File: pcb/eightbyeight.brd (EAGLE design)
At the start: 60 x 60 mm, 140 parts, among them CON1 USB_MICROSMT+THRUHULE, Q1 16MHz, SW1 SWITCH_SPDT, SW2 BRIGHTNESS, U1 MK20DN64VFM5, U10 FDG6316P, U11 FDG6316P, U12 FDG6316P, U2 ICN2026, U3 74138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

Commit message: Update board TODOs
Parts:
- R11: value 50 -> 47
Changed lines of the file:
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@@
 <layer number="13" name="Route13" color="4" fill="5" visible="no" active="no"/>
 <layer number="14" name="Route14" color="1" fill="6" visible="no" active="no"/>
-<layer number="15" name="Route" color="5" fill="1" visible="no" active="yes"/>
+<layer number="15" name="Route" color="5" fill="1" visible="yes" active="yes"/>
 <layer number="16" name="Bottom" color="1" fill="1" visible="no" active="yes"/>
 <layer number="17" name="Pads" color="10" fill="1" visible="yes" active="yes"/>
-<layer number="18" name="Vias" color="10" fill="1" visible="no" active="yes"/>
+<layer number="18" name="Vias" color="10" fill="1" visible="yes" active="yes"/>
 <layer number="19" name="Unrouted" color="6" fill="1" visible="no" active="yes"/>
 <layer number="20" name="Dimension" color="15" fill="1" visible="yes" active="yes"/>
@@
 <attribute name="VALUE" x="4.2" y="12.284" size="1.016" layer="27" rot="R180"/>
 </element>
-<element name="R11" library="adafruit" package="R0805" value="50" x="12" y="4.8" smashed="yes" rot="R180">
+<element name="R11" library="adafruit" package="R0805" value="47" x="12" y="4.8" smashed="yes" rot="R180">
 <attribute name="NAME" x="12.762" y="3.784" size="1.27" layer="25" rot="R180"/>
 <attribute name="VALUE" x="10.262" y="5.386" size="1.27" layer="27" rot="R180"/>

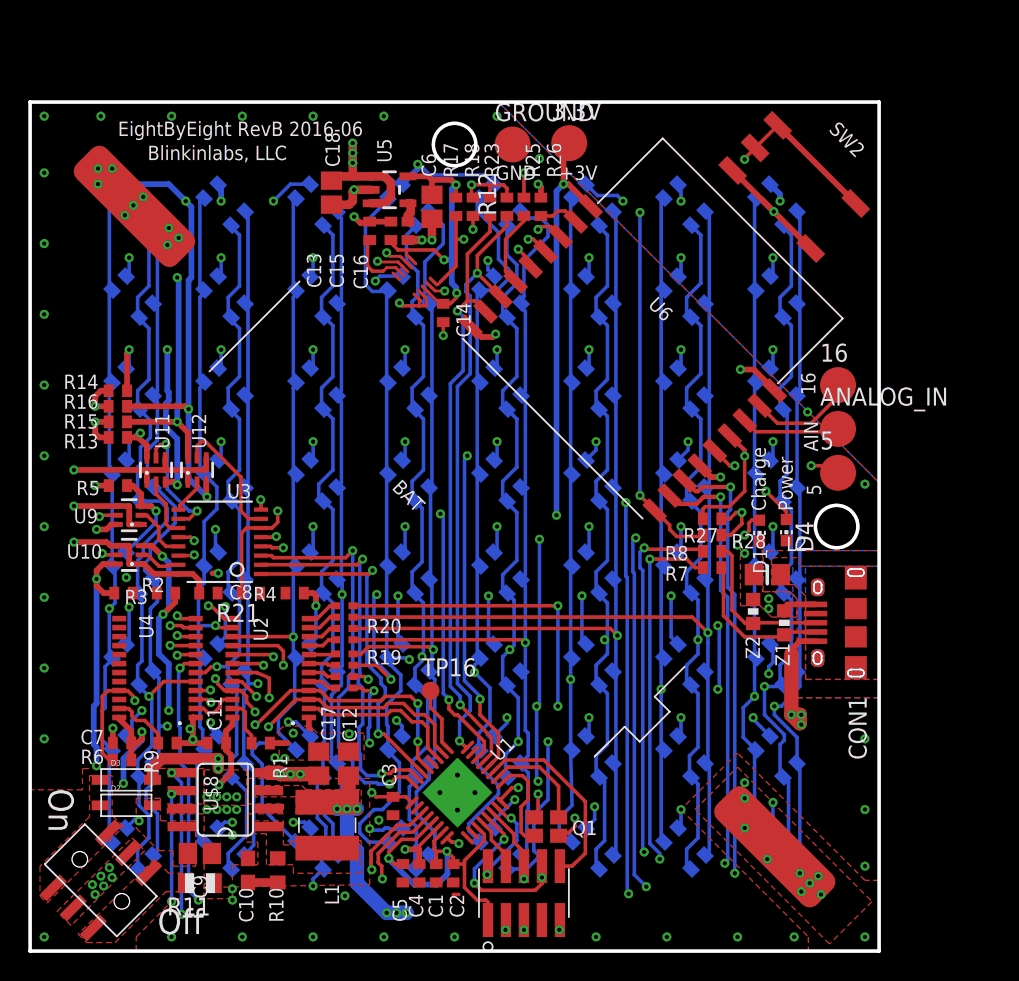
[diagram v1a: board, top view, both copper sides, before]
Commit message: Test pads in progress
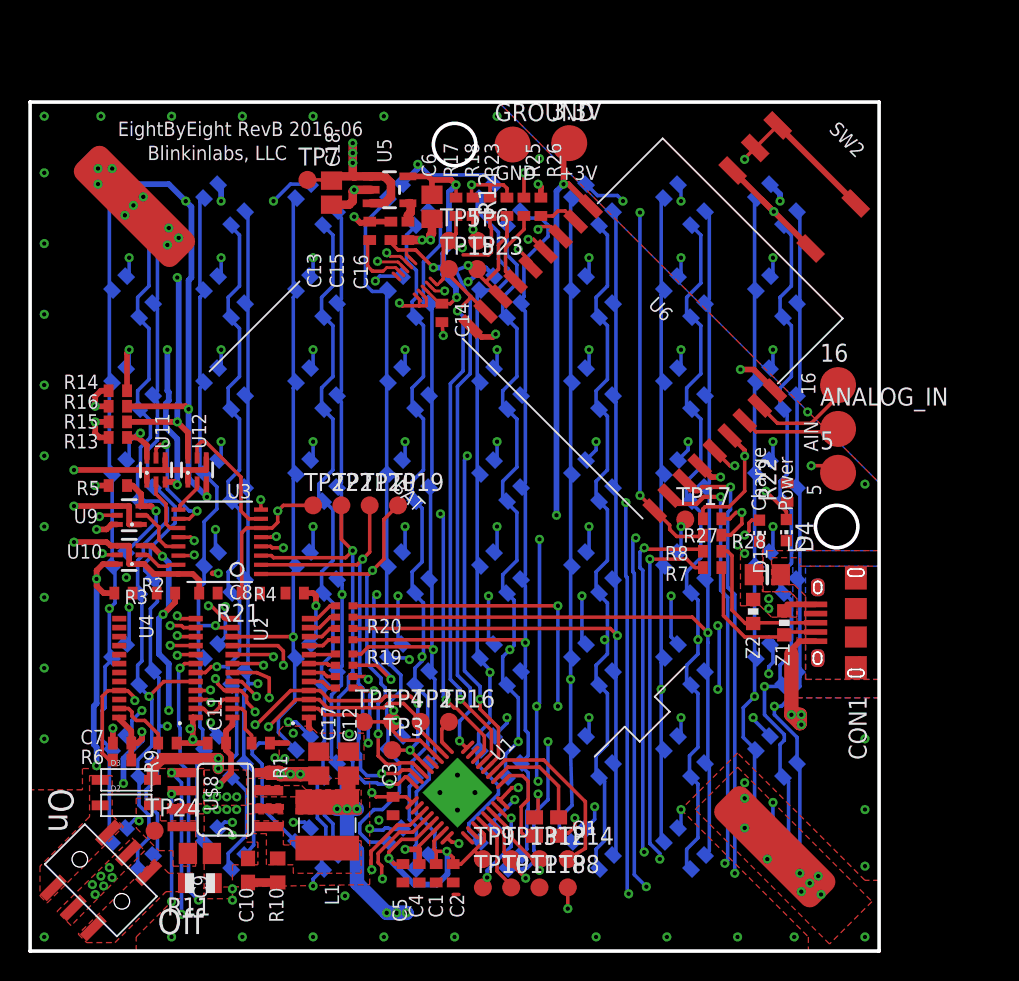
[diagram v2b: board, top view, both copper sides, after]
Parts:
- removed U$2: JTAG_ARM_10PIN, blinkinlabs:2X05-1.27MM-SMD
- added R22: 100, adafruit:R0402
- added TP1, TP10, TP11, TP12, TP13, TP14, TP15, TP17, TP18, TP19, TP2, TP20, TP21, TP22, TP23, TP24, TP3, TP4, TP5, TP6, TP7, TP8, TP9: PTR1B1,27, testpad:B1,27
- C16: value 470pF -> 47pF
- D1: value BLUE -> ORANGE
- D4: value BLUE -> PURPLE
- R12, R23, R25, R26, R27, R6: value 10k -> 47k
- R21: value 2k 1% -> 47k
- R28: value 10k -> DNP
- moved TP16 2.56 mm to (29.6, 16.2)
- moved C14 0.10 mm to (29.1, 45.1)
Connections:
- new net N$1: D1.C, D4.C, R22.2
- net +5V: now also TP7.TP
- net ARM_3V3: now also TP9.TP; no longer U$2.P$1
- net ARM_RESET: now also TP14.TP; no longer U$2.P$10
- net ARM_RX: now also TP13.TP; no longer U$2.P$8
- net ARM_RX1: now also TP23.TP
- net ARM_TCK: now also TP11.TP; no longer U$2.P$4
- net ARM_TMS: now also TP10.TP; no longer U$2.P$2
- net ARM_TX: now also TP12.TP; no longer U$2.P$6
- net BOOST_5V: now also TP24.TP
- net ESP_GPIO0: now also TP15.TP
- net ESP_RESET: now also TP17.TP
- net GND: now also R22.1, TP18.TP; no longer D1.C, D4.C, U$2.P$3, U$2.P$5, U$2.P$9
- net I2C_SCL: now also TP6.TP
- net I2C_SDA: now also TP5.TP
- net LED_CLK: now also TP2.TP
- net LED_DAT_0: now also TP1.TP
- net LED_HS_EN: now also TP22.TP
- net LED_OE: now also TP4.TP
- net LED_ROW_A: now also TP19.TP
- net LED_ROW_B: now also TP20.TP
- net LED_ROW_C: now also TP21.TP
- net LED_STB: now also TP3.TP
- net VBAT: now also TP8.TP
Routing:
- net LED_ROW_A: track 24.7 -> 31.0 mm
- net ARM_RX: track 57.4 -> 51.7 mm, vias 5 -> 3
- net ARM_3V3: track 68.5 -> 64.2 mm
- net LED_ROW_B: track 27.1 -> 31.2 mm
- net LED_ROW_C: track 28.1 -> 31.6 mm
- net LED_HS_EN: track 38.3 -> 40.9 mm
- net ARM_RX1: track 42.6 -> 45.0 mm
- net ARM_BOOTLOADER: track 4.49 -> 2.16 mm
- net GND: track 92.7 -> 90.8 mm, vias 91 -> 88
- net +5V: track 138.6 -> 140.3 mm
- net LED_STB: track 23.2 -> 24.8 mm
- net ARM_TCK: track 3.74 -> 5.40 mm
- net VBAT: track 45.1 -> 46.6 mm, vias 15 -> 16
- net ARM_TX: track 50.6 -> 49.4 mm
- net LED_DAT_0: track 11.6 -> 10.5 mm
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
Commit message: Closer to RevD
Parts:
- removed L2: 130ohm @100MHz, blinkinlabs:0805
- removed R22: 100, adafruit:R0402
- added SJ1: SOLDERJUMPERTRACE, SparkFun-Passives:SJ_2S-TRACE
- added TP25: PTR1B1,27, testpad:B1,27
- added Z3: PGB1010603, PaxInstrument-T400:SPARKFUN-RESISTORS_0603-RES
- moved Z2 0.47 mm to (51.0, 24.4)
- moved Z1 0.45 mm to (53.1, 23.6)
- moved TP17 0.30 mm to (46.0, 30.5)
- moved TP15 0.22 mm to (29.8, 48.3)
- moved TP23 0.22 mm to (31.8, 48.3)
- moved TP5 0.22 mm to (29.8, 50.3)
- moved TP6 0.22 mm to (31.8, 50.3)
- moved D1 0.20 mm to (51.5, 29.9)
- moved D4 0.20 mm to (53.5, 29.9)
- moved TP1 0.10 mm to (23.7, 16.2)
- moved TP16 0.10 mm to (29.7, 16.2)
- moved TP2 0.10 mm to (27.7, 16.2)
- moved TP3 0.10 mm to (25.7, 14.2)
- moved TP4 0.10 mm to (25.7, 16.2)
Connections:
- removed net BUTTON1: R28.1, SW2.1, SW2.2, U6.IO4
- removed net SHIELD: CON1.PAD$1, CON1.PAD$10, CON1.PAD$2, CON1.PAD$3, CON1.PAD$4, CON1.PAD$5, CON1.PAD$6, CON1.PAD$7, CON1.PAD$8, CON1.PAD$9, L2.1
- new net BUTTON: R28.1, SW2.1, SW2.2, TP25.TP, U6.IO4
- net GND: now also CON1.PAD$1, CON1.PAD$10, CON1.PAD$2, CON1.PAD$3, CON1.PAD$4, CON1.PAD$5, CON1.PAD$6, CON1.PAD$7, CON1.PAD$8, CON1.PAD$9, SJ1.1, Z3.1; no longer L2.2, R22.1
- net N$1: now also SJ1.2; no longer R22.2
- net USB_5V: now also Z3.2
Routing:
- net BUTTON: track 0.00 -> 45.3 mm, vias 0 -> 3
- net BUTTON1: track 44.5 -> 0.00 mm, vias 3 -> 0
- net GND: track 90.8 -> 74.9 mm, vias 88 -> 94
- net N$1: track 0.00 -> 3.69 mm
- net BCOL2: track 56.4 -> 54.6 mm
- net ESP_RESET: track 51.6 -> 53.1 mm
- net USB_D-: track 52.3 -> 51.0 mm
- net USB_D+: track 52.2 -> 51.0 mm
- net 1ROW1: track 74.3 -> 73.1 mm
- net ESP_GPIO0: track 44.0 -> 45.3 mm
- net ARM_RX1: track 45.0 -> 43.9 mm
- net N$9: track 11.2 -> 10.3 mm
- net RCOL3: track 54.5 -> 55.3 mm
- net ACC_INT1: track 14.2 -> 15.0 mm
- net BCOL6: track 79.0 -> 79.7 mm
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- removed copper zone on layer 1, net SHIELD
- removed copper zone on layer 16, net SHIELD
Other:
- board text added: "EightByEight RevD 2016-07"
- board text removed: "EightByEight RevB 2016-06"

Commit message: Final RevD
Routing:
- net GND: vias 94 -> 104
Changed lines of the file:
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@@
 <via x="58.9" y="28.3" extent="1-16" drill="0.3"/>
 <via x="55.1" y="28.2" extent="1-16" drill="0.3"/>
+<via x="17.2" y="37.8" extent="1-16" drill="0.3"/>
+<via x="23.6" y="44.8" extent="1-16" drill="0.3"/>
+<via x="32.7" y="37.4" extent="1-16" drill="0.3"/>
+<via x="36.2" y="44.6" extent="1-16" drill="0.3"/>
+<via x="49.2" y="40" extent="1-16" drill="0.3"/>
+<via x="36" y="31.9" extent="1-16" drill="0.3"/>
+<via x="26.1" y="26.2" extent="1-16" drill="0.3"/>
+<via x="36.7" y="19.9" extent="1-16" drill="0.3"/>
+<via x="39.1" y="11.8" extent="1-16" drill="0.3"/>
+<via x="45.5" y="11.2" extent="1-16" drill="0.3"/>
 </signal>
 <signal name="LED_STB">

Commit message: Clean up board silkscreen
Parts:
- R1: value 2k 1% -> 1.8k 1%
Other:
- board text added: "3.3V"
- board text removed: "+3V"

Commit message: Small updates from further testing
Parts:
- R1: value 1.8k 1% -> 1.6k 1%
- R12, R23, R25, R26, R27: value 47k -> 10k
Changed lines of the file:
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@@
 <layer number="13" name="Route13" color="4" fill="5" visible="no" active="no"/>
 <layer number="14" name="Route14" color="1" fill="6" visible="no" active="no"/>
-<layer number="15" name="Route" color="5" fill="1" visible="no" active="yes"/>
-<layer number="16" name="Bottom" color="1" fill="1" visible="no" active="yes"/>
-<layer number="17" name="Pads" color="10" fill="1" visible="no" active="yes"/>
-<layer number="18" name="Vias" color="10" fill="1" visible="no" active="yes"/>
+<layer number="15" name="Route" color="5" fill="1" visible="yes" active="yes"/>
+<layer number="16" name="Bottom" color="1" fill="1" visible="yes" active="yes"/>
+<layer number="17" name="Pads" color="10" fill="1" visible="yes" active="yes"/>
+<layer number="18" name="Vias" color="10" fill="1" visible="yes" active="yes"/>
 <layer number="19" name="Unrouted" color="6" fill="1" visible="no" active="yes"/>
 <layer number="20" name="Dimension" color="15" fill="1" visible="yes" active="yes"/>
@@
 <layer number="25" name="tNames" color="11" fill="1" visible="no" active="yes"/>
 <layer number="26" name="bNames" color="7" fill="1" visible="no" active="yes"/>
-<layer number="27" name="tValues" color="11" fill="1" visible="yes" active="yes"/>
+<layer number="27" name="tValues" color="11" fill="1" visible="no" active="yes"/>
 <layer number="28" name="bValues" color="7" fill="1" visible="no" active="yes"/>
-<layer number="29" name="tStop" color="7" fill="3" visible="no" active="yes"/>
+<layer number="29" name="tStop" color="7" fill="3" visible="yes" active="yes"/>
 <layer number="30" name="bStop" color="7" fill="6" visible="no" active="yes"/>
 <layer number="31" name="tCream" color="7" fill="4" visible="no" active="yes"/>
@@
 <attribute name="VALUE" x="5.235" y="15.605" size="1.016" layer="27" rot="R180"/>
 </element>
-<element name="R1" library="adafruit" package="R0402" value="1.8k 1%" x="16.3" y="14.7" smashed="yes" rot="R180">
+<element name="R1" library="adafruit" package="R0402" value="1.6k 1%" x="16.3" y="14.7" smashed="yes" rot="R180">
 <attribute name="NAME" x="16.065" y="13.062" size="1.016" layer="25"/>
 <attribute name="VALUE" x="17.168" y="13.835" size="1.016" layer="27" rot="R270"/>
@@
 <attribute name="VALUE" x="21.195" y="49.335" size="1.016" layer="27" rot="R270"/>
 </element>
-<element name="R23" library="adafruit" package="R0402" value="47k" x="32.5" y="52.6" smashed="yes" rot="R90">
+<element name="R23" library="adafruit" package="R0402" value="10k" x="32.5" y="52.6" smashed="yes" rot="R90">
 <attribute name="NAME" x="33.138" y="54.665" size="1.016" layer="25" rot="R90"/>
 <attribute name="VALUE" x="33.132" y="54.665" size="1.016" layer="27" rot="R90"/>
 </element>
-<element name="R25" library="adafruit" package="R0402" value="47k" x="34.9" y="52.6" smashed="yes" rot="R270">
+<element name="R25" library="adafruit" package="R0402" value="10k" x="34.9" y="52.6" smashed="yes" rot="R270">
 <attribute name="NAME" x="36.038" y="54.665" size="1.016" layer="25" rot="R90"/>
 <attribute name="VALUE" x="36.032" y="54.765" size="1.016" layer="27" rot="R90"/>
 </element>
-<element name="R26" library="adafruit" package="R0402" value="47k" x="36.1" y="52.6" smashed="yes" rot="R90">
+<element name="R26" library="adafruit" package="R0402" value="10k" x="36.1" y="52.6" smashed="yes" rot="R90">
 <attribute name="NAME" x="37.538" y="54.665" size="1.016" layer="25" rot="R90"/>
 <attribute name="VALUE" x="37.532" y="54.665" size="1.016" layer="27" rot="R90"/>
 </element>
-<element name="R27" library="adafruit" package="R0402" value="47k" x="48.2" y="30.55" smashed="yes">
+<element name="R27" library="adafruit" package="R0402" value="10k" x="48.2" y="30.55" smashed="yes">
 <attribute name="NAME" x="49.835" y="32.188" size="1.016" layer="25" rot="R180"/>
 <attribute name="VALUE" x="44.465" y="30.118" size="1.016" layer="27"/>
@@
 <attribute name="NAME" x="59.03" y="36.551" size="1.016" layer="25"/>
 </element>
-<element name="R12" library="adafruit" package="R0402" value="47k" x="33.7" y="52.6" smashed="yes" rot="R90">
+<element name="R12" library="adafruit" package="R0402" value="10k" x="33.7" y="52.6" smashed="yes" rot="R90">
 <attribute name="NAME" x="34.438" y="54.665" size="1.016" layer="25" rot="R90"/>
 <attribute name="VALUE" x="34.632" y="54.665" size="1.016" layer="27" rot="R90"/>

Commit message: RevE.A
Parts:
- removed 16, 3.3V, 5, ANALOG_IN, GROUND: PTR1B2,54, testpad:B2,54
- added U$10, U$2, U$6, U$9: TEST_POINT, DevicesToMerge:IO_HOLE_3MM
- R13, R14, R15, R16, R2, R3, R4, R5: value 2k -> 4.7k
- R21, R6: value 47k -> 10k
- moved R12 0.10 mm to (33.7, 52.5)
- moved R17 0.10 mm to (30.1, 52.5)
- moved R18 0.10 mm to (31.3, 52.5)
- moved R23 0.10 mm to (32.5, 52.5)
- moved R25 0.10 mm to (34.9, 52.5)
- moved R26 0.10 mm to (36.1, 52.5)
- renumbered BAT to J2, CON1 to J1, U$8 to U7
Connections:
- net +3V3: now also U$10.1; no longer 3.3V.TP
- net ESP_GPIO16: now also U$9.1; no longer 16.TP
- net ESP_TOUT: no longer ANALOG_IN.TP
- net EXP_GPIO5: now also U$6.1; no longer 5.TP
- net GND: now also U$2.1; no longer GROUND.TP
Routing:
- net ESP_TOUT: track 7.15 -> 1.12 mm
- net 1ROW7: track 94.6 -> 91.6 mm, vias 9 -> 10
- net +3V3: track 83.1 -> 81.2 mm, vias 8 -> 6
- net ESP_GPIO16: track 7.84 -> 6.08 mm
- net EXP_GPIO5: track 9.37 -> 10.8 mm
- net GND: track 74.5 -> 73.3 mm, vias 104 -> 102
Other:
- outline, holes or cut-outs redrawn
- board text added: "EightByEight RevE 2016-07"
- board text removed: "AIN"
- board text removed: "EightByEight RevD 2016-07"

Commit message: Rev E, as submitted
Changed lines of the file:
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@@
 <via x="45.5" y="11.2" extent="1-16" drill="0.3"/>
 <contactref element="U$2" pad="1"/>
-<wire x1="50.5" y1="55.95" x2="50.45" y2="55.95" width="0.254" layer="2"/>
-<wire x1="50.45" y1="55.95" x2="50" y2="55.5" width="0.254" layer="2"/>
-<wire x1="50" y1="55.5" x2="50" y2="41.3" width="0.254" layer="2"/>
-<wire x1="50" y1="41.3" x2="50.2" y2="41.1" width="0.254" layer="2"/>
 <via x="32.6" y="26.2" extent="1-16" drill="0.3"/>
+<wire x1="50.5" y1="55.95" x2="50.2" y2="55.65" width="0.254" layer="16"/>
+<wire x1="50.2" y1="55.65" x2="50" y2="55.45" width="0.254" layer="16"/>
+<wire x1="50" y1="55.45" x2="50" y2="53.1" width="0.254" layer="16"/>
+<wire x1="50" y1="53.1" x2="50.2" y2="52.9" width="0.254" layer="16"/>
+<wire x1="50.2" y1="52.9" x2="50.2" y2="41.1" width="0.254" layer="16"/>
 </signal>
 <signal name="LED_STB">
